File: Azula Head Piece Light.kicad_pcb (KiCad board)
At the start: 2 copper layers, 35.8 x 18 mm, 11 parts, among them SW1 SW_DIP_x03

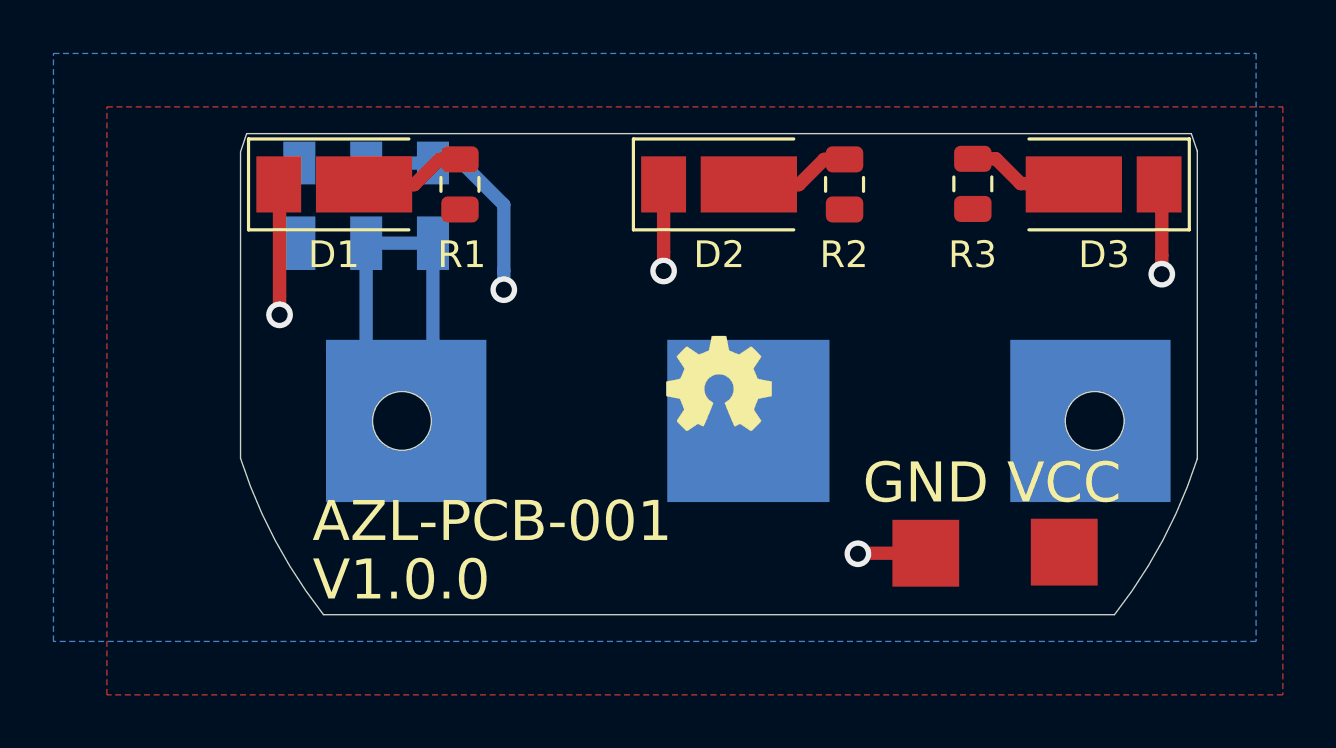
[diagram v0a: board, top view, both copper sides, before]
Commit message: Fix LED orientation and switch wiring
Fix LED orientation and switch wiring
Version 1.0.1
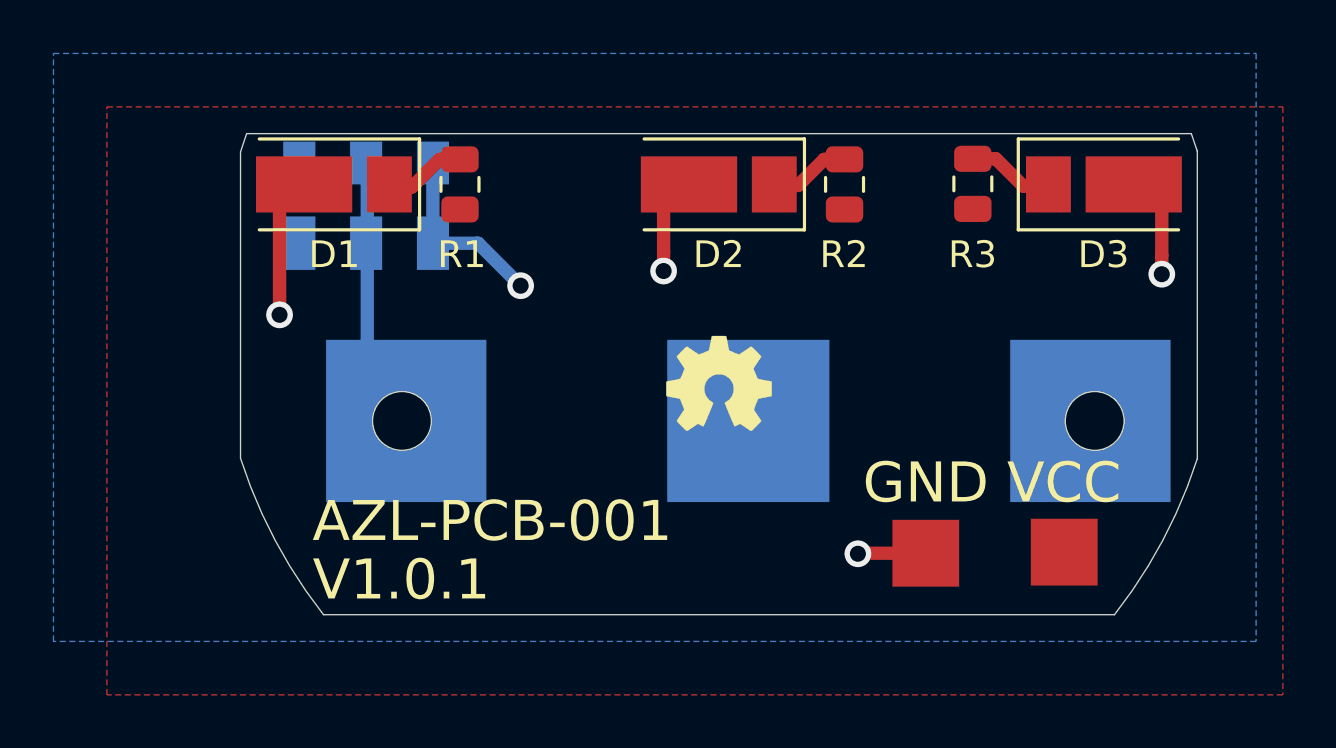
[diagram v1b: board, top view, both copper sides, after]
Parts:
- turned D1 to 180 degrees
- turned D2 to 180 degrees
- turned D3 to 0 degrees
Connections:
- BT1 pad 1: /BATSWITCH -> /BAT+
- BT1 pad 3: (no net) -> Net-(BT1-Pad3)
- D1 pad 1: GND -> Net-(D1-Pad1)
- D1 pad 2: Net-(D1-Pad2) -> GND
- D2 pad 1: GND -> Net-(D2-Pad1)
- D2 pad 2: Net-(D2-Pad2) -> GND
- D3 pad 1: GND -> Net-(D3-Pad1)
- D3 pad 2: Net-(D3-Pad2) -> GND
- R1 pad 2: Net-(D1-Pad2) -> Net-(D1-Pad1)
- R2 pad 2: Net-(D2-Pad2) -> Net-(D2-Pad1)
- R3 pad 2: Net-(D3-Pad2) -> Net-(D3-Pad1)
- SW1 pad 1: (no net) -> Net-(SW1-Pad1)
- SW1 pad 2: +3V0 -> /BAT+
- SW1 pad 4: (no net) -> Net-(SW1-Pad4)
- SW1 pad 5: /BATSWITCH -> /BAT+
- SW1 pad 6: /BATSWITCH -> +3V0
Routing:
- net /BATSWITCH: track 11.9 -> 0.00 mm
- net /BAT+: track 0.00 -> 7.45 mm
- net Net-(D3-Pad2): track 4.53 -> 0.00 mm
- net Net-(D1-Pad2): track 4.19 -> 0.00 mm
- net Net-(D2-Pad2): track 3.82 -> 0.00 mm
- net Net-(D3-Pad1): track 0.00 -> 3.26 mm
- net Net-(D1-Pad1): track 0.00 -> 3.11 mm
- net Net-(D2-Pad1): track 0.00 -> 2.98 mm
- net +3V0: track 8.98 -> 7.19 mm
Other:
- board text added: "V1.0.1"
- board text removed: "V1.0.0"

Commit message: Fixed pin out on LED
Fixed pin out on LED
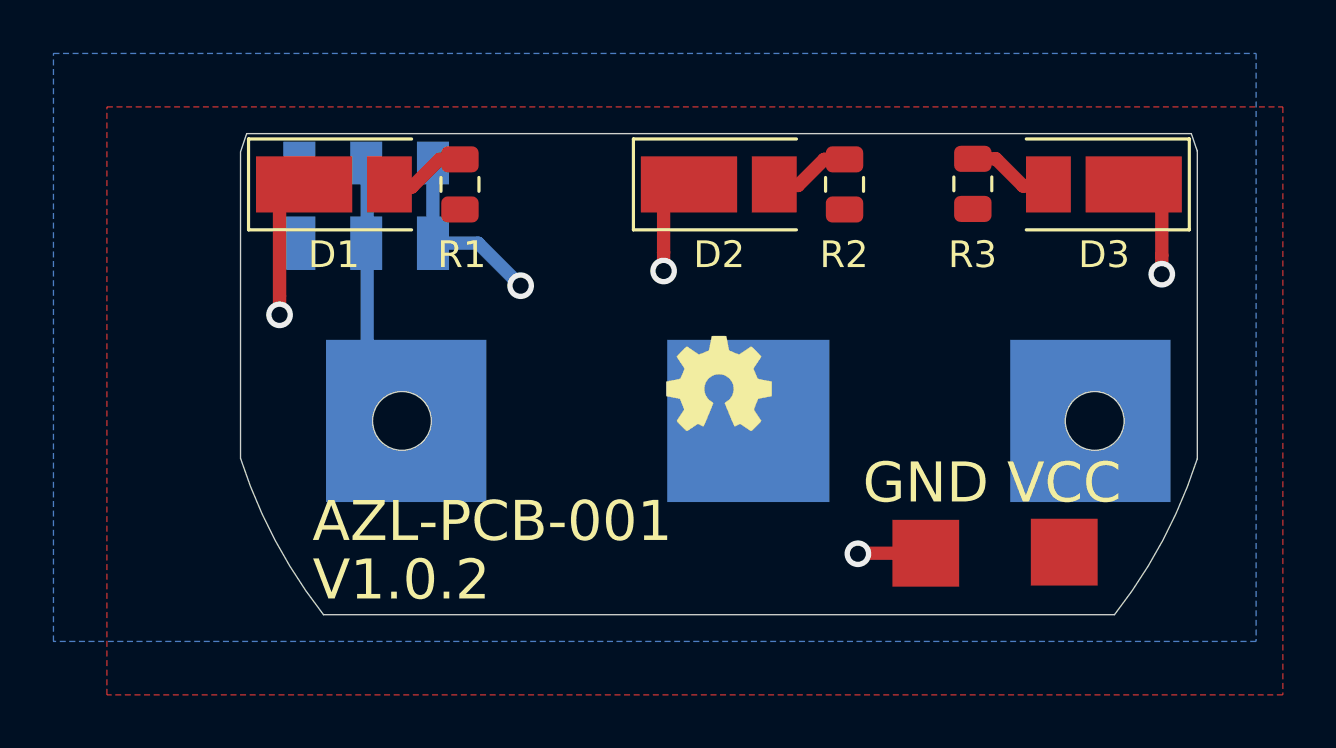
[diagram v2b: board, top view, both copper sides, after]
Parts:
- turned D1 to 0 degrees
- turned D2 to 0 degrees
- turned D3 to 180 degrees
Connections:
- BT1 pad 3: Net-(BT1-Pad3) -> (no net)
- D1 pad 1: Net-(D1-Pad1) -> GND
- D1 pad 2: GND -> Net-(D1-Pad2)
- D2 pad 1: Net-(D2-Pad1) -> GND
- D2 pad 2: GND -> Net-(D2-Pad2)
- D3 pad 1: Net-(D3-Pad1) -> GND
- D3 pad 2: GND -> Net-(D3-Pad2)
- R1 pad 2: Net-(D1-Pad1) -> Net-(D1-Pad2)
- R2 pad 2: Net-(D2-Pad1) -> Net-(D2-Pad2)
- R3 pad 2: Net-(D3-Pad1) -> Net-(D3-Pad2)
- SW1 pad 1: Net-(SW1-Pad1) -> (no net)
- SW1 pad 4: Net-(SW1-Pad4) -> (no net)
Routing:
- net Net-(D3-Pad2): track 0.00 -> 3.26 mm
- net Net-(D3-Pad1): track 3.26 -> 0.00 mm
- net Net-(D1-Pad2): track 0.00 -> 3.11 mm
- net Net-(D1-Pad1): track 3.11 -> 0.00 mm
- net Net-(D2-Pad2): track 0.00 -> 2.98 mm
- net Net-(D2-Pad1): track 2.98 -> 0.00 mm
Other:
- board text added: "V1.0.2"
- board text removed: "V1.0.1"

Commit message: Added fiducials
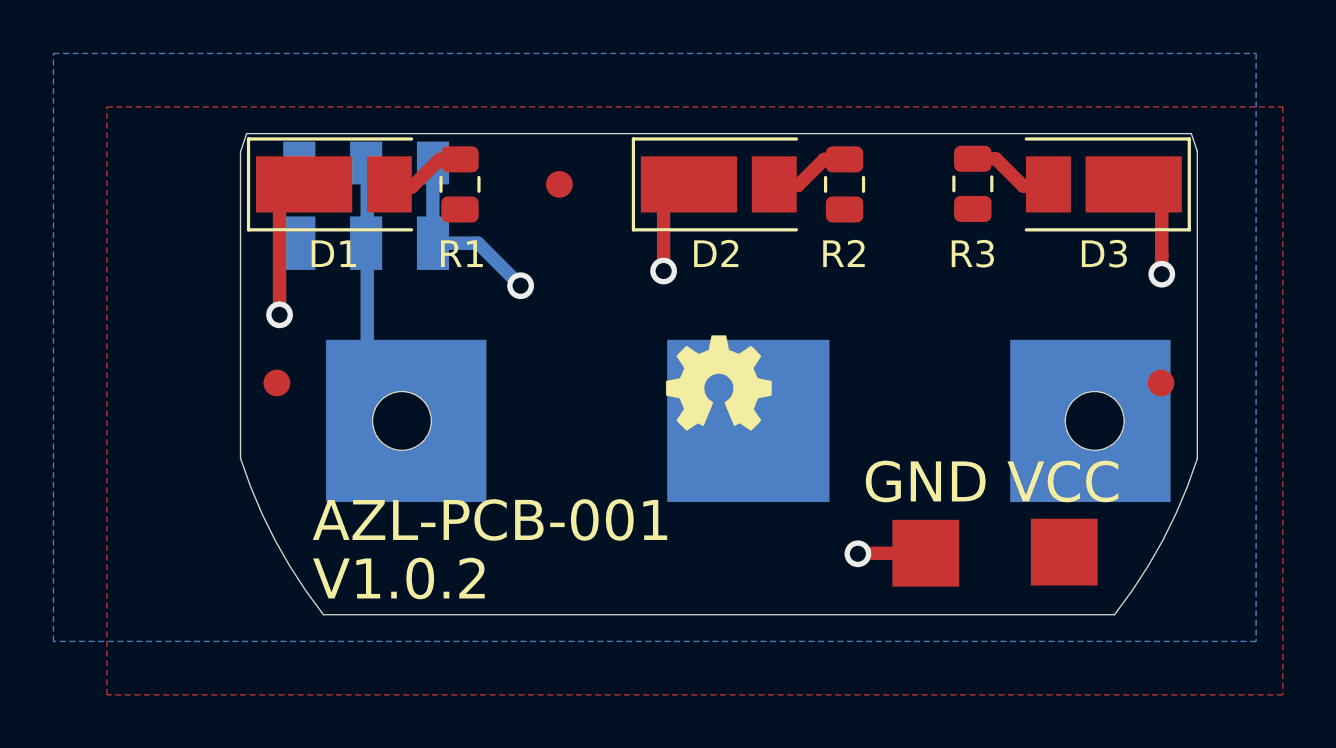
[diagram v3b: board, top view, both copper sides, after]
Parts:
- added FID1: Fiducial, Fiducial_LE:Fiducial_1mm_Mask2mm, F.Cu at (111.9, 133.9)
- added FID2: Fiducial, Fiducial_LE:Fiducial_1mm_Mask2mm, F.Cu at (134.4, 141.3)
- added FID3: Fiducial, Fiducial_LE:Fiducial_1mm_Mask2mm, F.Cu at (101.4, 141.3)
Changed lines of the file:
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@@
     (tracks 29)
     (zones 0)
-    (modules 11)
+    (modules 14)
     (nets 7)
   )
@@
   (layers
     (0 F.Cu signal)
-    (31 B.Cu signal)
+    (31 B.Cu signal hide)
     (32 B.Adhes user)
     (33 F.Adhes user)
@@
     (aux_axis_origin 0 0)
     (grid_origin 100 150)
-    (visible_elements 7FFFFFFF)
+    (visible_elements 7FFEFFFF)
     (pcbplotparams
       (layerselection 0x310fc_ffffffff)
@@
     (uvia_drill 0.1)
     (add_net /BAT+)
+    (add_net "Net-(BT1-Pad3)")
     (add_net "Net-(D1-Pad2)")
     (add_net "Net-(D2-Pad2)")
     (add_net "Net-(D3-Pad2)")
+    (add_net "Net-(SW1-Pad1)")
+    (add_net "Net-(SW1-Pad4)")
   )
   (net_class Power ""
@@
     (add_net +3V0)
     (add_net GND)
+  )
+  (module Fiducial_LE:Fiducial_1mm_Mask2mm (layer F.Cu)
+    (at 101.36 141.33)
+    (descr "Circular Fiducial, 1mm bare copper, 2mm soldermask opening (Level A)")
+    (tags fiducial)
+    (attr smd)
+    (fp_text reference FID3 (at 0 -2) (layer F.Fab)
+      (effects (font (size 1 1) (thickness 0.15)))
+    )
+    (fp_text value Fiducial (at 0 2) (layer F.Fab)
+      (effects (font (size 1 1) (thickness 0.15)))
+    )
+    (fp_circle (center 0 0) (end 1 0) (layer F.Fab) (width 0.1))
+    (fp_text user %R (at 0 0) (layer F.Fab)
+      (effects (font (size 0.4 0.4) (thickness 0.06)))
+    )
+    (fp_circle (center 0 0) (end 1.25 0) (layer F.CrtYd) (width 0.05))
+    (pad "" smd circle (at 0 0) (size 1 1) (layers F.Cu F.Mask)
+      (solder_mask_margin 0.5) (clearance 0.5))
+  )
+  (module Fiducial_LE:Fiducial_1mm_Mask2mm (layer F.Cu)
+    (at 134.44 141.33)
+    (descr "Circular Fiducial, 1mm bare copper, 2mm soldermask opening (Level A)")
+    (tags fiducial)
+    (attr smd)
+    (fp_text reference FID2 (at 0 -2) (layer F.Fab)
+      (effects (font (size 1 1) (thickness 0.15)))
+    )
+    (fp_text value Fiducial (at 0 2) (layer F.Fab)
+      (effects (font (size 1 1) (thickness 0.15)))
+    )
+    (fp_circle (center 0 0) (end 1.25 0) (layer F.CrtYd) (width 0.05))
+    (fp_text user %R (at 0 0) (layer F.Fab)
+      (effects (font (size 0.4 0.4) (thickness 0.06)))
+    )
+    (fp_circle (center 0 0) (end 1 0) (layer F.Fab) (width 0.1))
+    (pad "" smd circle (at 0 0) (size 1 1) (layers F.Cu F.Mask)
+      (solder_mask_margin 0.5) (clearance 0.5))
+  )
+  (module Fiducial_LE:Fiducial_1mm_Mask2mm (layer F.Cu)
+    (at 111.93 133.9)
+    (descr "Circular Fiducial, 1mm bare copper, 2mm soldermask opening (Level A)")
+    (tags fiducial)
+    (attr smd)
+    (fp_text reference FID1 (at 0 -2) (layer F.Fab)
+      (effects (font (size 1 1) (thickness 0.15)))
+    )
+    (fp_text value Fiducial (at 0 2) (layer F.Fab)
+      (effects (font (size 1 1) (thickness 0.15)))
+    )
+    (fp_circle (center 0 0) (end 1 0) (layer F.Fab) (width 0.1))
+    (fp_text user %R (at 0 0) (layer F.Fab)
+      (effects (font (size 0.4 0.4) (thickness 0.06)))
+    )
+    (fp_circle (center 0 0) (end 1.25 0) (layer F.CrtYd) (width 0.05))
+    (pad "" smd circle (at 0 0) (size 1 1) (layers F.Cu F.Mask)
+      (solder_mask_margin 0.5) (clearance 0.5))
   )
   (module "Azula Head Piece Light:LED_JB5630AWT-P-H40GA0000-NZ000001" (layer F.Cu)
@@
     (at 117.9 133.9)
     (attr smd)
-    (fp_text reference D2 (at 0.01 2.63) (layer F.SilkS)
+    (fp_text reference D2 (at -0.1 2.63) (layer F.SilkS)
       (effects (font (size 1 1) (thickness 0.15)))
     )
@@
   )
   (module Logos_LE:OSHW-Symbol_4mm_Silkscreen (layer F.Cu)
-    (at 117.9 141.35)
+    (at 117.894157 141.33)
     (fp_text reference L1 (at -0.12 -2.53) (layer F.Fab) hide
       (effects (font (size 1 1) (thickness 0.15)))
@@
   (segment (start 101.46 138.072894) (end 101.46 138.78) (width 0.5) (layer F.Cu) (net 2))
   (segment (start 101.46 133.76) (end 101.46 138.072894) (width 0.5) (layer F.Cu) (net 2))
+  (segment (start 104.74 133.05) (end 104.74 140.5) (width 0.5) (layer B.Cu) (net 3))
   (segment (start 106.41 134) (end 105.53 134) (width 0.5) (layer F.Cu) (net 4))
   (segment (start 108.21 132.9625) (end 107.4475 132.9625) (width 0.5) (layer F.Cu) (net 4))
@@
   (segment (start 127.4 132.9425) (end 128.2625 132.9425) (width 0.5) (layer F.Cu) (net 6))
   (segment (start 128.2625 132.9425) (end 129.28 133.96) (width 0.5) (layer F.Cu) (net 6))
-  (segment (start 104.74 133.05) (end 104.74 140.5) (width 0.5) (layer B.Cu) (net 3))
   (zone (net 2) (net_name GND) (layer B.Cu) (hatch edge 0.508)
     (connect_pads (clearance 0.4))
